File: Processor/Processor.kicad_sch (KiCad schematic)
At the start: 43 parts, among them J1 Buss, J2 L2|L3, U1 MC6800, U10 74LS573, U11 74LS573, U2 74LS74, U3 74LS00, U4 74LS245, U5 74LS573, U6 74LS138, U7 GAL20V8, U8 74LS04, U9 74LS573, Y1 2.0MHz

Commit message: churn
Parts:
- removed J2: L2|L3, Connector_PinSocket_2.54mm:PinSocket_2x08_P2.54mm_Horizontal, symbol Connector_Generic:Conn_02x08_Odd_Even
- added J2: L2, Connector_PinHeader_2.54mm:PinHeader_1x10_P2.54mm_Horizontal, symbol Connector:Conn_01x10_Pin
- added J3: L3, Connector_PinHeader_2.54mm:PinHeader_1x10_P2.54mm_Horizontal, symbol Connector:Conn_01x10_Pin
- U11, U5: now fitted
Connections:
- net +5V: now also J2.1 (Pin_1), J3.1 (Pin_1)
- net A10: now also RN3.4 (R3); no longer RN3.7 (R6)
- net A11: now also RN3.5 (R4); no longer RN3.6 (R5)
- net A12: now also RN3.6 (R5); no longer RN3.5 (R4)
- net A13: now also RN3.7 (R6); no longer RN3.4 (R3)
- net A14: now also RN3.8 (R7); no longer RN3.3 (R2)
- net A15: now also RN3.9 (R8); no longer RN3.2 (R1)
- net A8: now also RN3.2 (R1); no longer RN3.9 (R8)
- net A9: now also RN3.3 (R2); no longer RN3.8 (R7)
- net GND: now also J2.10 (Pin_10), J3.10 (Pin_10)
- net at U11.12 (Q7): now also J3.9 (Pin_9)
- net at U11.13 (Q6): now also J3.8 (Pin_8)
- net at U11.14 (Q5): now also J3.7 (Pin_7)
- net at U11.15 (Q4): now also J3.6 (Pin_6)
- net at U11.16 (Q3): now also J3.5 (Pin_5)
- net at U11.17 (Q2): now also J3.4 (Pin_4)
- net at U11.18 (Q1): now also J3.3 (Pin_3)
- net at U11.19 (Q0): now also J3.2 (Pin_2)
- net at U5.12 (Q7): now also J2.9 (Pin_9)
- net at U5.13 (Q6): now also J2.8 (Pin_8)
- net at U5.14 (Q5): now also J2.7 (Pin_7)
- net at U5.15 (Q4): now also J2.6 (Pin_6)
- net at U5.16 (Q3): now also J2.5 (Pin_5)
- net at U5.17 (Q2): now also J2.4 (Pin_4)
- net at U5.18 (Q1): now also J2.3 (Pin_3)
- net at U5.19 (Q0): now also J2.2 (Pin_2)

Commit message: a bunch of stuff
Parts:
- removed C10, C11, C5, C9: 100n, Capacitor_THT:C_Disc_D3.0mm_W1.6mm_P2.50mm, symbol Device:C
- removed D1: S0, LED_THT:LED_Rectangular_W5.0mm_H2.0mm, symbol Device:LED_Small
- removed D2: S1, LED_THT:LED_Rectangular_W5.0mm_H2.0mm, symbol Device:LED_Small
- removed D3: S2, LED_THT:LED_Rectangular_W5.0mm_H2.0mm, symbol Device:LED_Small
- removed D4: S3, LED_THT:LED_Rectangular_W5.0mm_H2.0mm, symbol Device:LED_Small
- removed D5: S4, LED_THT:LED_Rectangular_W5.0mm_H2.0mm, symbol Device:LED_Small
- removed D6: S5, LED_THT:LED_Rectangular_W5.0mm_H2.0mm, symbol Device:LED_Small
- removed D7: S6, LED_THT:LED_Rectangular_W5.0mm_H2.0mm, symbol Device:LED_Small
- removed D8: S7, LED_THT:LED_Rectangular_W5.0mm_H2.0mm, symbol Device:LED_Small
- removed J2: L2, Connector_PinHeader_2.54mm:PinHeader_1x10_P2.54mm_Horizontal, symbol Connector:Conn_01x10_Pin
- removed J3: L3, Connector_PinHeader_2.54mm:PinHeader_1x10_P2.54mm_Horizontal, symbol Connector:Conn_01x10_Pin
- removed RN5: 220Ω, Resistor_THT:R_Array_SIP9, symbol Device:R_Network08
- removed U10, U11, U5, U9: 74LS573, Package_DIP:DIP-20_W7.62mm, symbol 74xx:74LS573
- removed U6: 74LS138, Package_DIP:DIP-16_W7.62mm, symbol 74xx:74LS138
- added G1: Logo, 0-Footprints:Crank, symbol 0-Symbols:Logo
- U7: value GAL20V8 -> GAL22V10; symbol 0-Symbols:GAL20V8 -> 0-Symbols:GAL22V10
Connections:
- net ~{LATCH_SEL} is gone; now on net GND: U7.17 (I/O)
- net A10: now also U7.9 (I); no longer U7.13 (I/~{OE})
- net A11: now also U7.8 (I); no longer U7.11 (I)
- net A12: now also U7.7 (I); no longer U7.10 (I)
- net A13: now also U7.6 (I); no longer U7.9 (I)
- net A14: now also U7.5 (I); no longer U7.8 (I)
- net A15: now also U7.4 (I); no longer U7.7 (I)
- net A8: now also U7.11 (I); no longer U7.23 (I)
- net A9: now also U7.10 (I); no longer U7.14 (I)
- net BUS_OK: now also U7.19 (I/O); no longer U7.18 (I/O)
- net GND: now also U3.10, U3.12, U3.13, U3.9, U7.13 (I), U7.14 (I/O), U7.18 (I/O), U8.11, U8.13; no longer U7.3 (I), U7.4 (I), U7.5 (I), U7.6 (I)
- net VMA: now also U7.3 (I)
- net ~{BANK_SEL}: now also U7.21 (I/O); no longer U7.20 (I/O)
- net ~{IO_SEL}: now also U7.20 (I/O); no longer U7.19 (I/O)
- net ~{RAM_SEL}: now also U7.23 (I/0); no longer U7.22 (I/O)
- net ~{ROM_SEL}: now also U7.22 (I/O); no longer U7.21 (I/O)
- net Φ2: now also J1.B3 (Φ2); no longer J1.44
- net BANK_0: no longer names the net of J1.10
- net BANK_1: no longer names the net of J1.12
- net BANK_2: no longer names the net of J1.14
- net BANK_3: no longer names the net of J1.16
- net BANK_4: no longer names the net of J1.18
- net BANK_5: no longer names the net of J1.20
- net BANK_6: no longer names the net of J1.22
- net BANK_7: no longer names the net of J1.24
- net LOAD_0: no longer names the net of U3.11
- net LOAD_1: no longer names the net of U3.8
- net LOAD_2: no longer names the net of U8.10
- net LOAD_3: no longer names the net of U8.12
- no-connect marks 16 -> 17
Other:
- moved on the sheet: R7, R8, R9, RN3, U2B, U3C, U3D, U7, U8E, U8F

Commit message: ordered v01 of the cpu
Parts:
- removed C6, C7, C8: 100n, Capacitor_THT:C_Disc_D3.0mm_W1.6mm_P2.50mm, symbol Device:C
- removed R6: 10K, Resistor_THT:R_Axial_DIN0204_L3.6mm_D1.6mm_P5.08mm_Horizontal, symbol Device:R
- removed RN1, RN2, RN3, RN4: 4.7K, Resistor_THT:R_Array_SIP9, symbol Device:R_Network08
- removed U2: 74LS74, Package_DIP:DIP-14_W7.62mm, symbol 74xx:74LS74
- removed U3: 74LS00, Package_DIP:DIP-14_W7.62mm, symbol 74xx:74LS00
- removed U8: 74LS04, Package_DIP:DIP-14_W7.62mm, symbol 74xx:74LS04
- added C5: 100n, 0-Footprints:C_Disc_D5.0mm_W2.5mm_P5.00mm, symbol Device:C
- added G2: Crankery, 0-Footprints:crankery_small, symbol 0-Symbols:Logo
- added G3: Motorola, 0-Footprints:Motorola, symbol 0-Symbols:Logo
- added G4: Crank, 0-Footprints:Crank, symbol 0-Symbols:Logo
- added R1, R2, R3, R4, R9: 10K, 0-Footprints:R_Axial_DIN0204_L3.6mm_D1.6mm_P7.62mm_Horizontal, symbol Device:R
- added RN1, RN2, RN3, RN4, RN5, RN6, RN7, RN8: 4.7K, 0-Footprints:R_Array_SIP5, symbol Device:R_Network04
- added U2: MC6875, 0-Footprints:DIP-16_W7.62mm, symbol 0-Symbols:MC6875
- C1: value 100n -> 100nF; footprint Capacitor_THT:C_Disc_D3.0mm_W1.6mm_P2.50mm -> 0-Footprints:C_Disc_D5.0mm_W2.5mm_P5.00mm
- C2, C3, C4: footprint Capacitor_THT:C_Disc_D3.0mm_W1.6mm_P2.50mm -> 0-Footprints:C_Disc_D5.0mm_W2.5mm_P5.00mm
- G1: value Logo -> Crank
- R5, R7, R8: footprint Resistor_THT:R_Axial_DIN0204_L3.6mm_D1.6mm_P5.08mm_Horizontal -> 0-Footprints:R_Axial_DIN0204_L3.6mm_D1.6mm_P7.62mm_Horizontal
- R6: renamed from R9; footprint Resistor_THT:R_Axial_DIN0204_L3.6mm_D1.6mm_P5.08mm_Horizontal -> 0-Footprints:R_Axial_DIN0204_L3.6mm_D1.6mm_P7.62mm_Horizontal
- U1: value MC6800 -> M6800; footprint Package_DIP:DIP-40_W15.24mm -> 0-Footprints:DIP-40_W15.24mm
- U4: footprint Package_DIP:DIP-20_W7.62mm -> 0-Footprints:DIP-20_W7.62mm
- U7: footprint Package_DIP:DIP-24_W7.62mm -> 0-Footprints:DIP-24_W7.62mm
- Y1: value 2.0MHz -> 4.000MHz; footprint Oscillator:Oscillator_DIP-14 -> 0-Footprints:Oscillator_DIP-14
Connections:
- net ~{DBE} is gone; now on net DBE: U1.36 (DBE)
- net +5V: now also C1.2, C2.2, C3.2, C4.2, J1.P1 (+5V), R1.1, R2.1, R3.1, R4.1, R9.1, RN1.1 (common), RN2.1 (common), RN3.1 (common), RN4.1 (common), RN5.1 (common), RN6.1 (common), RN7.1 (common), RN8.1 (common), U2.16 (VCC); no longer C1.1, C2.1, C3.1, C4.1, J1.VCC (-12V)
- net A0: now also RN3.5 (R4)
- net A1: now also RN3.4 (R3)
- net A10: now also RN5.4 (R3)
- net A11: now also RN5.5 (R4)
- net A12: now also RN6.2 (R1)
- net A13: now also RN6.3 (R2)
- net A14: now also RN6.4 (R3)
- net A15: now also RN6.5 (R4)
- net A2: now also RN3.3 (R2)
- net A3: now also RN3.2 (R1)
- net A4: now also RN7.2 (R1)
- net A5: now also RN7.3 (R2)
- net A6: now also RN7.4 (R3)
- net A7: now also RN7.5 (R4)
- net A8: now also RN5.2 (R1)
- net A9: now also RN5.3 (R2)
- net BD0: now also RN8.5 (R4)
- net BD1: now also RN8.4 (R3)
- net BD2: now also RN8.3 (R2)
- net BD3: now also RN8.2 (R1)
- net BD4: now also RN2.5 (R4)
- net BD5: now also RN2.4 (R3)
- net BD6: now also RN2.3 (R2)
- net BD7: now also RN2.2 (R1)
- net D0: now also RN1.5 (R4)
- net D1: now also RN1.4 (R3)
- net D2: now also RN1.3 (R2)
- net D3: now also RN1.2 (R1)
- net D4: now also RN4.5 (R4)
- net D5: now also RN4.4 (R3)
- net D6: now also RN4.3 (R2)
- net D7: now also RN4.2 (R1)
- net GND: now also C1.1, C2.1, C3.1, C4.1, J1.P2 (GND), C5.2, U2.1 (X1), U2.8 (GND); no longer C1.2, C2.2, C3.2, C4.2, J1.GND
- net R/~{W}: now also R2.2; no longer R5.2
- net ~{HALT}: now also R3.2
- net ~{RESET}: now also R9.2, U2.14 (~{RESET})
- net Φ1: now also U2.15 (MPU_Φ1)
- net Φ2: now also U2.7 (BUS_Φ2); no longer U1.37 (Phi2)
- net MEM_CLK: now reaches J1.36 (MEM_CLK)
- net MEM_CLK: now also U2.9 (MEM_CLK)
- net DMA_GRANT: now reaches J1.38 (DMA_GRANT)
- net DMA_GRANT: now also U2.11 (DMA_GRANT)
- net MEMRDY: now reaches J1.40 (MEMRDY)
- net MEMRDY: now also R5.2, U2.6 (MEMRDY)
- net ~{DMA_REQ}: now reaches J1.42 (~{DMA_REQ})
- net ~{DMA_REQ}: now also R1.2, U2.10 (~{DMA_RQ})
- net ~{POR}: now reaches J1.44 (~{POR})
- net ~{POR}: now also C5.1, R4.2, U2.12 (~{POR})
- net 2.0MHz: no longer names the net of Y1.8 (OUT)
- net 2.0MHz: now also U2.3 (EXT_IN)
- new net: U1.37 (Phi2), U2.13 (MCU_Φ2)
- no-connect marks 17 -> 18
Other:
- moved on the sheet: C2, C3, C4, R6, R7, R8, U1, U4, U7, Y1

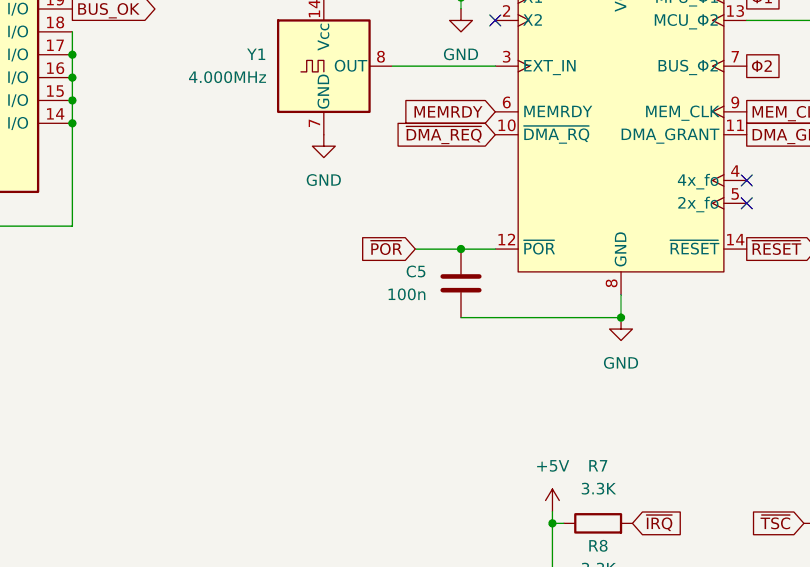
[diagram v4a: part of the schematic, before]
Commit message: lots of fixes to stack handling on emu, fix the latches on the banked memory board, tons of little bug fixes
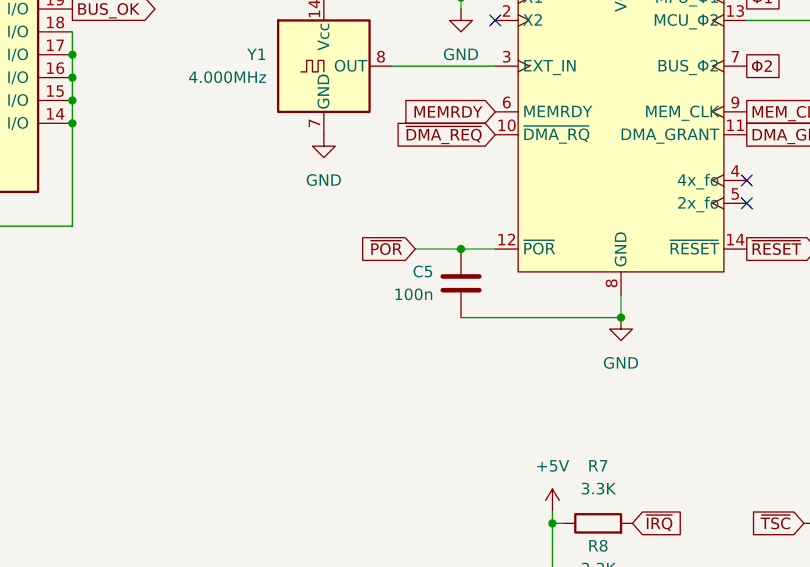
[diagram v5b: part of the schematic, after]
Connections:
- net GND: now also C5.1; no longer C5.2
- net ~{POR}: now also C5.2; no longer C5.1
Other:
- moved on the sheet: C5
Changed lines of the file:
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@@
 	)
 	(junction
-		(at 162.56 93.98)
+		(at 257.81 50.8)
 		(diameter 0)
 		(color 0 0 0 0)
 	)
 	(junction
-		(at 257.81 50.8)
+		(at 279.4 151.13)
 		(diameter 0)
 		(color 0 0 0 0)
 	)
 	(junction
-		(at 279.4 151.13)
+		(at 162.56 93.98)
 		(diameter 0)
 		(color 0 0 0 0)
@@
 	(wire
 		(pts
-			(xy 162.56 93.98) (xy 166.37 93.98)
-		)
-		(stroke
-			(width 0)
-			(type default)
-		)
-	)
-	(wire
-		(pts
 			(xy 294.64 166.37) (xy 275.59 166.37)
 		)
@@
 	(wire
 		(pts
+			(xy 162.56 93.98) (xy 166.37 93.98)
+		)
+		(stroke
+			(width 0)
+			(type default)
+		)
+	)
+	(wire
+		(pts
 			(xy 255.27 38.1) (xy 255.27 48.26)
 		)
@@
 	(symbol
 		(lib_id "Device:C")
-		(at 162.56 97.79 0)
-		(mirror y)
+		(at 162.56 97.79 180)
 		(unit 1)
 		(body_style 1)
@@
 		(dnp no)
 		(property "Reference" "C5"
-			(at 158.75 96.5199 0)
+			(at 159.512 96.52 0)
 			(show_name no)
 			(do_not_autoplace no)
@@
 		)
 		(property "Value" "100n"
-			(at 158.75 99.0599 0)
+			(at 159.512 99.06 0)
 			(show_name no)
 			(do_not_autoplace no)
@@
 		)
 		(property "Footprint" "0-Footprints:C_Disc_D5.0mm_W2.5mm_P5.00mm"
-			(at 161.5948 101.6 0)
+			(at 161.5948 93.98 0)
 			(hide yes)
 			(show_name no)
